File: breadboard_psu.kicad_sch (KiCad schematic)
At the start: 21 parts, among them J1 Barrel_Jack_MountingPin, J2 Conn_01x02, J3 Conn_01x02, J4 Conn_02x04_Odd_Even, J5 Conn_01x02, SW1 SW_DPDT_x2, SW2 SW_DPDT_x2, U1 LM317_TO-220

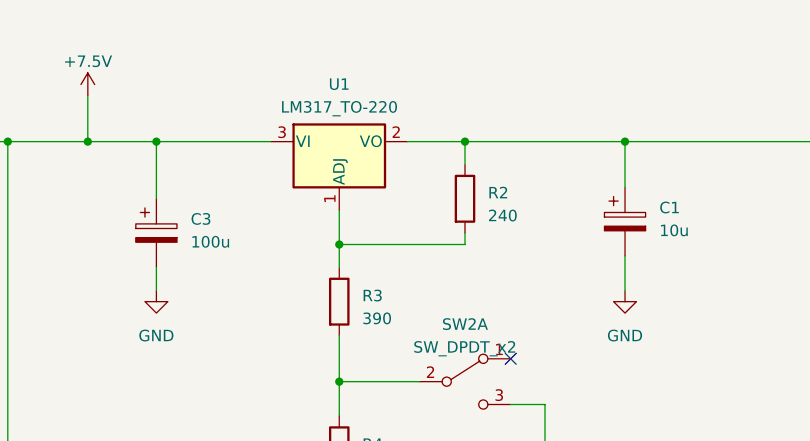
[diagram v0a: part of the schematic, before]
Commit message: MaJ TO220 a plat + esthétique
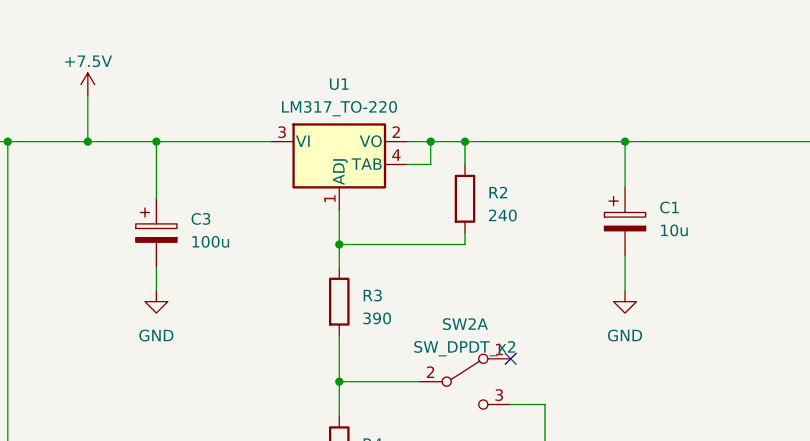
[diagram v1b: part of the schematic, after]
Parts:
- J1: footprint Connector_BarrelJack:BarrelJack_Kycon_KLDX-0202-xC_Horizontal -> Connector_BarrelJack:BarrelJack_Horizontal_PJ-002A
- U1: footprint Package_TO_SOT_THT:TO-220-3_Vertical -> Package_TO_SOT_THT:TO-220-3_Horizontal_TabDown_Connected; symbol Regulator_Linear:LM317_TO-220 -> MyLibrary:LM317_TO-220_TAB
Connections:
- net VCC: now also U1.4 (TAB)
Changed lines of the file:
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@@
     (company "Julien Boriasse")
+  )
+  (junction (at 170.18 88.9) (diameter 0) (color 0 0 0 0)
   )
   (junction (at 72.39 181.61) (diameter 0) (color 0 0 0 0)
@@
     (stroke (width 0) (type default))
   )
-  (wire (pts (xy 167.64 88.9) (xy 173.99 88.9))
+  (wire (pts (xy 167.64 88.9) (xy 170.18 88.9))
     (stroke (width 0) (type default))
   )
@@
     (stroke (width 0) (type default))
   )
+  (wire (pts (xy 170.18 91.44) (xy 170.18 88.9))
+    (stroke (width 0) (type default))
+  )
   (wire (pts (xy 281.94 88.9) (xy 255.27 88.9))
     (stroke (width 0) (type default))
@@
     (stroke (width 0) (type default))
   )
+  (wire (pts (xy 167.64 91.44) (xy 170.18 91.44))
+    (stroke (width 0) (type default))
+  )
   (wire (pts (xy 160.02 129.54) (xy 160.02 127))
     (stroke (width 0) (type default))
@@
   )
   (wire (pts (xy 123.19 125.73) (xy 123.19 88.9))
+    (stroke (width 0) (type default))
+  )
+  (wire (pts (xy 170.18 88.9) (xy 173.99 88.9))
     (stroke (width 0) (type default))
   )
@@
       (effects (font (size 1.27 1.27)))
     )
-    (property "Footprint" "Connector_BarrelJack:BarrelJack_Kycon_KLDX-0202-xC_Horizontal" (at 49.53 89.916 0)
+    (property "Footprint" "Connector_BarrelJack:BarrelJack_Horizontal_PJ-002A" (at 49.53 89.916 0)
       (effects (font (size 1.27 1.27)) hide)
     )
@@
     )
   )
-  (symbol (lib_id "Regulator_Linear:LM317_TO-220") (at 160.02 88.9 0) (unit 1)
+  (symbol (lib_id "MyLibrary:LM317_TO-220_TAB") (at 160.02 88.9 0) (unit 1)
     (in_bom yes) (on_board yes) (dnp no) (fields_autoplaced)
     (property "Reference" "U1" (at 160.02 82.55 0)
@@
       (effects (font (size 1.27 1.27)))
     )
-    (property "Footprint" "Package_TO_SOT_THT:TO-220-3_Vertical" (at 160.02 82.55 0)
+    (property "Footprint" "Package_TO_SOT_THT:TO-220-3_Horizontal_TabDown_Connected" (at 160.02 82.55 0)
       (effects (font (size 1.27 1.27) italic) hide)
     )
@@
     (pin "2")
     (pin "3")
-    (instances
-      (project "breadboard_psu"
+    (pin "4")
+    (instances
+      (project "breadboard_psu"

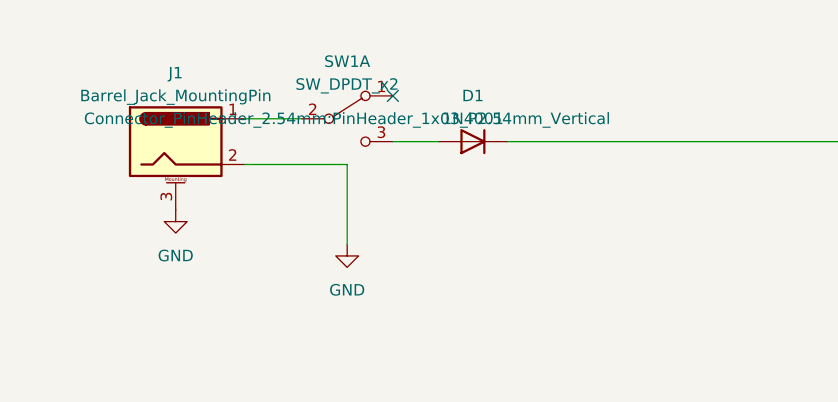
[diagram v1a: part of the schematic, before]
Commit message: Ajout MPN + BOM
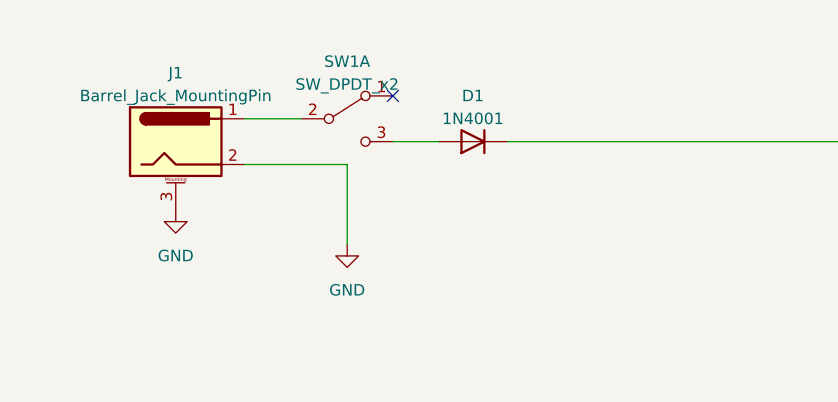
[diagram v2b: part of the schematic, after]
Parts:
- C1: SPN (none) -> 1189-3733-1-ND
- C2: SPN (none) -> BC1084CT-ND
- C3: SPN (none) -> 399-6650-1-ND
- D1: MPN (none) -> 1N4001-T; SPN (none) -> 1N4001DICT-ND
- J1: MPN (none) -> PJ-002A; SPN (none) -> CP-002A-ND
- U1: MPN (none) -> LM317KCS; SPN (none) -> 296-13869-5-ND
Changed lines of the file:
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@@
     )
     (property "Footprint" "Connector_PinHeader_2.54mm:PinHeader_1x03_P2.54mm_Vertical" (at 67.31 86.36 0)
-      (effects (font (size 1.27 1.27)))
+      (effects (font (size 1.27 1.27)) hide)
     )
     (property "Datasheet" "~" (at 67.31 86.36 0)
@@
       (effects (font (size 1.27 1.27)) hide)
     )
+    (property "MPN" "1N4001-T" (at 81.28 88.9 0)
+      (effects (font (size 1.27 1.27)) hide)
+    )
+    (property "SPN" "1N4001DICT-ND" (at 81.28 88.9 0)
+      (effects (font (size 1.27 1.27)) hide)
+    )
     (pin "1")
     (pin "2")
@@
       (effects (font (size 1.27 1.27)) hide)
     )
+    (property "SPN" "1189-3733-1-ND" (at 191.77 97.79 0)
+      (effects (font (size 1.27 1.27)) hide)
+    )
     (pin "1")
     (pin "2")
@@
       (effects (font (size 1.27 1.27)) hide)
     )
-    (property "Datasheet" "~" (at 49.53 89.916 0)
+    (property "Datasheet" "https://www.cuidevices.com/product/resource/pj-002a.pdf" (at 49.53 89.916 0)
+      (effects (font (size 1.27 1.27)) hide)
+    )
+    (property "SPN" "CP-002A-ND" (at 48.26 88.9 0)
+      (effects (font (size 1.27 1.27)) hide)
+    )
+    (property "MPN" "PJ-002A" (at 48.26 88.9 0)
       (effects (font (size 1.27 1.27)) hide)
     )
@@
       (effects (font (size 1.27 1.27)) hide)
     )
+    (property "SPN" "BC1084CT-ND" (at 215.9 97.79 0)
+      (effects (font (size 1.27 1.27)) hide)
+    )
     (pin "1")
     (pin "2")
@@
     )
     (property "Height" "12.50mm" (at 139.7 99.06 0)
+      (effects (font (size 1.27 1.27)) hide)
+    )
+    (property "SPN" "399-6650-1-ND" (at 139.7 99.06 0)
       (effects (font (size 1.27 1.27)) hide)
     )
@@
       (effects (font (size 1.27 1.27)) hide)
     )
+    (property "MPN" "LM317KCS" (at 160.02 88.9 0)
+      (effects (font (size 1.27 1.27)) hide)
+    )
+    (property "SPN" "296-13869-5-ND" (at 160.02 88.9 0)
+      (effects (font (size 1.27 1.27)) hide)
+    )

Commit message: DEL 5mm
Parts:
- D2: footprint LED_THT:LED_D3.0mm -> LED_THT:LED_D5.0mm
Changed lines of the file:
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@@
       (effects (font (size 1.27 1.27)) (justify right))
     )
-    (property "Footprint" "LED_THT:LED_D3.0mm" (at 232.41 104.14 0)
+    (property "Footprint" "LED_THT:LED_D5.0mm" (at 232.41 104.14 0)
       (effects (font (size 1.27 1.27)) hide)
     )

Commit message: 4 pin par tab
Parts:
- removed J2, J3: Conn_01x02, Connector_PinHeader_2.54mm:PinHeader_1x02_P2.54mm_Vertical, symbol Connector_Generic:Conn_01x02
- added J2, J3: Conn_02x02_Odd_Even, Connector_PinHeader_2.54mm:PinHeader_2x02_P2.54mm_Vertical, symbol Connector_Generic:Conn_02x02_Odd_Even
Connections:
- net GND: now also J2.3 (Pin_3), J2.4 (Pin_4), J3.3 (Pin_3), J3.4 (Pin_4)
- net VCC: now also J2.1 (Pin_1), J2.2 (Pin_2), J3.1 (Pin_1), J3.2 (Pin_2)

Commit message: Info des composants a jour
MPN SPN footprint 3D
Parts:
- C1: footprint Capacitor_THT:CP_Radial_D5.0mm_P2.50mm -> Library:CP_Radial_D5.0mm_P5.0mm_EEU-EB1J100SB; Height 8mm -> 12mm; MPN 35ML10MEFCT54X7 -> EEU-EB1J100SB; SPN 1189-3733-1-ND -> P19615CT-ND
- C2: footprint Capacitor_THT:C_Axial_L3.8mm_D2.6mm_P7.50mm_Horizontal -> Library:C_Rect_L4.0mm_W2.5mm_P5.00mm_RDER71H104K0K1H03B; MPN K104K15X7RF5TL2 -> RDER71H104K0K1H03B; SPN BC1084CT-ND -> 490-8814-ND
- C3: Height 12.50mm -> 5mm; MPN ESK107M025AE3EA -> ES5107M016AE1EA; SPN 399-6650-1-ND -> 399-6648-1-ND
- D1: MPN 1N4001-T -> 1N4001RLG; SPN 1N4001DICT-ND -> 1N4001RLGOSTR-ND
- D2: MPN (none) -> XLUG12D; SPN (none) -> 1497-1023-ND
- R2: SPN (none) -> 13-MFR-25FBF52-240R-ND
- R3: SPN (none) -> MFR-25FBF52-390R-ND
- R4: SPN (none) -> MFR-25FBF52-330R-ND
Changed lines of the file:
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@@
       (effects (font (size 1.27 1.27)) hide)
     )
-    (property "Datasheet" "~" (at 232.41 104.14 0)
+    (property "Datasheet" "https://www.sunledusa.com/products/spec/XLUG12D.pdf" (at 232.41 104.14 0)
+      (effects (font (size 1.27 1.27)) hide)
+    )
+    (property "SPN" "1497-1023-ND" (at 232.41 104.14 90)
+      (effects (font (size 1.27 1.27)) hide)
+    )
+    (property "MPN" "XLUG12D" (at 232.41 104.14 90)
       (effects (font (size 1.27 1.27)) hide)
     )
@@
       (effects (font (size 1.27 1.27)) hide)
     )
-    (property "Datasheet" "http://www.vishay.com/docs/88503/1n4001.pdf" (at 81.28 88.9 0)
+    (property "Datasheet" "https://www.onsemi.com/pdf/datasheet/1n4001-d.pdf" (at 81.28 88.9 0)
       (effects (font (size 1.27 1.27)) hide)
     )
@@
       (effects (font (size 1.27 1.27)) hide)
     )
-    (property "MPN" "1N4001-T" (at 81.28 88.9 0)
-      (effects (font (size 1.27 1.27)) hide)
-    )
-    (property "SPN" "1N4001DICT-ND" (at 81.28 88.9 0)
+    (property "MPN" "1N4001RLG" (at 81.28 88.9 0)
+      (effects (font (size 1.27 1.27)) hide)
+    )
+    (property "SPN" "1N4001RLGOSTR-ND" (at 81.28 88.9 0)
       (effects (font (size 1.27 1.27)) hide)
     )
@@
     )
     (property "Datasheet" "~" (at 160.02 106.68 0)
+      (effects (font (size 1.27 1.27)) hide)
+    )
+    (property "SPN" "MFR-25FBF52-390R-ND" (at 160.02 106.68 0)
       (effects (font (size 1.27 1.27)) hide)
     )
@@
       (effects (font (size 1.27 1.27)) (justify left))
     )
-    (property "Footprint" "Capacitor_THT:CP_Radial_D5.0mm_P2.50mm" (at 192.7352 101.6 0)
-      (effects (font (size 1.27 1.27)) hide)
-    )
-    (property "Datasheet" "~" (at 191.77 97.79 0)
-      (effects (font (size 1.27 1.27)) hide)
-    )
-    (property "MPN" "35ML10MEFCT54X7" (at 191.77 97.79 0)
-      (effects (font (size 1.27 1.27)) hide)
-    )
-    (property "Height" "8mm" (at 191.77 97.79 0)
-      (effects (font (size 1.27 1.27)) hide)
-    )
-    (property "SPN" "1189-3733-1-ND" (at 191.77 97.79 0)
+    (property "Footprint" "Library:CP_Radial_D5.0mm_P5.0mm_EEU-EB1J100SB" (at 192.7352 101.6 0)
+      (effects (font (size 1.27 1.27)) hide)
+    )
+    (property "Datasheet" "https://industrial.panasonic.com/cdbs/www-data/pdf/RDF0000/ABA0000C1024.pdf" (at 191.77 97.79 0)
+      (effects (font (size 1.27 1.27)) hide)
+    )
+    (property "MPN" "EEU-EB1J100SB" (at 191.77 97.79 0)
+      (effects (font (size 1.27 1.27)) hide)
+    )
+    (property "Height" "12mm" (at 191.77 97.79 0)
+      (effects (font (size 1.27 1.27)) hide)
+    )
+    (property "SPN" "P19615CT-ND" (at 191.77 97.79 0)
       (effects (font (size 1.27 1.27)) hide)
     )
@@
       (effects (font (size 1.27 1.27)) hide)
     )
+    (property "SPN" "13-MFR-25FBF52-240R-ND" (at 173.99 95.25 0)
+      (effects (font (size 1.27 1.27)) hide)
+    )
     (pin "1")
     (pin "2")
@@
       (effects (font (size 1.27 1.27)) (justify left))
     )
-    (property "Footprint" "Capacitor_THT:C_Axial_L3.8mm_D2.6mm_P7.50mm_Horizontal" (at 216.8652 101.6 0)
-      (effects (font (size 1.27 1.27)) hide)
-    )
-    (property "Datasheet" "~" (at 215.9 97.79 0)
-      (effects (font (size 1.27 1.27)) hide)
-    )
-    (property "MPN" "K104K15X7RF5TL2" (at 215.9 97.79 0)
-      (effects (font (size 1.27 1.27)) hide)
-    )
-    (property "SPN" "BC1084CT-ND" (at 215.9 97.79 0)
+    (property "Footprint" "Library:C_Rect_L4.0mm_W2.5mm_P5.00mm_RDER71H104K0K1H03B" (at 216.8652 101.6 0)
+      (effects (font (size 1.27 1.27)) hide)
+    )
+    (property "Datasheet" "https://search.murata.co.jp/Ceramy/image/img/A01X/G101/ENG/RDE_X7R_250V-1kV_E.pdf" (at 215.9 97.79 0)
+      (effects (font (size 1.27 1.27)) hide)
+    )
+    (property "MPN" "RDER71H104K0K1H03B" (at 215.9 97.79 0)
+      (effects (font (size 1.27 1.27)) hide)
+    )
+    (property "SPN" "490-8814-ND" (at 215.9 97.79 0)
       (effects (font (size 1.27 1.27)) hide)
     )
@@
       (effects (font (size 1.27 1.27)) hide)
     )
-    (property "MPN" "ESK107M025AE3EA" (at 139.7 99.06 0)
-      (effects (font (size 1.27 1.27)) hide)
-    )
-    (property "Height" "12.50mm" (at 139.7 99.06 0)
-      (effects (font (size 1.27 1.27)) hide)
-    )
-    (property "SPN" "399-6650-1-ND" (at 139.7 99.06 0)
+    (property "MPN" "ES5107M016AE1EA" (at 139.7 99.06 0)
+      (effects (font (size 1.27 1.27)) hide)
+    )
+    (property "Height" "5mm" (at 139.7 99.06 0)
+      (effects (font (size 1.27 1.27)) hide)
+    )
+    (property "SPN" "399-6648-1-ND" (at 139.7 99.06 0)
       (effects (font (size 1.27 1.27)) hide)
     )
@@
       (effects (font (size 1.27 1.27)) hide)
     )
+    (property "SPN" "MFR-25FBF52-330R-ND" (at 160.02 123.19 0)
+      (effects (font (size 1.27 1.27)) hide)
+    )

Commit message: Changement du silkscreen + Resistance & diode 300mils
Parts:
- D1: footprint Diode_THT:D_DO-41_SOD81_P10.16mm_Horizontal -> Diode_THT:D_DO-41_SOD81_P7.62mm_Horizontal
- R1, R2, R3, R4: footprint Resistor_THT:R_Axial_DIN0207_L6.3mm_D2.5mm_P10.16mm_Horizontal -> Resistor_THT:R_Axial_DIN0207_L6.3mm_D2.5mm_P7.62mm_Horizontal
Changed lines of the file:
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@@
       (effects (font (size 1.27 1.27)))
     )
-    (property "Footprint" "Diode_THT:D_DO-41_SOD81_P10.16mm_Horizontal" (at 81.28 88.9 0)
+    (property "Footprint" "Diode_THT:D_DO-41_SOD81_P7.62mm_Horizontal" (at 81.28 88.9 0)
       (effects (font (size 1.27 1.27)) hide)
     )
@@
       (effects (font (size 1.27 1.27)) (justify left))
     )
-    (property "Footprint" "Resistor_THT:R_Axial_DIN0207_L6.3mm_D2.5mm_P10.16mm_Horizontal" (at 158.242 106.68 90)
+    (property "Footprint" "Resistor_THT:R_Axial_DIN0207_L6.3mm_D2.5mm_P7.62mm_Horizontal" (at 158.242 106.68 90)
       (effects (font (size 1.27 1.27)) hide)
     )
@@
       (effects (font (size 1.27 1.27)) (justify left))
     )
-    (property "Footprint" "Resistor_THT:R_Axial_DIN0207_L6.3mm_D2.5mm_P10.16mm_Horizontal" (at 230.632 95.25 90)
+    (property "Footprint" "Resistor_THT:R_Axial_DIN0207_L6.3mm_D2.5mm_P7.62mm_Horizontal" (at 230.632 95.25 90)
       (effects (font (size 1.27 1.27)) hide)
     )
@@
       (effects (font (size 1.27 1.27)) (justify left))
     )
-    (property "Footprint" "Resistor_THT:R_Axial_DIN0207_L6.3mm_D2.5mm_P10.16mm_Horizontal" (at 172.212 95.25 90)
+    (property "Footprint" "Resistor_THT:R_Axial_DIN0207_L6.3mm_D2.5mm_P7.62mm_Horizontal" (at 172.212 95.25 90)
       (effects (font (size 1.27 1.27)) hide)
     )
@@
       (effects (font (size 1.27 1.27)) (justify left))
     )
-    (property "Footprint" "Resistor_THT:R_Axial_DIN0207_L6.3mm_D2.5mm_P10.16mm_Horizontal" (at 158.242 123.19 90)
-      (effects (font (size 1.27 1.27)) hide)
-    )
+    (property "Footprint" "Resistor_THT:R_Axial_DIN0207_L6.3mm_D2.5mm_P7.62mm_Horizontal" (at 158.242 123.19 90)
+      (effects (font (size 1.27 1.27)) hide)
+    )

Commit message: Cleanup
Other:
- note added: "VCC = 5V ou 3.3V selon la position du jumper sur SW2"
- note removed: "VCC = 5V or 3.3V depending on ADJ"
- title: Breadboard PSU -> Carte d'alimentation de prototypage
- moved on the sheet: C1, C2, C3, D1, D2, H1, H2, H3, H4, J1, J2, J3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

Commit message: Footprint oversized
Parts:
- C3: footprint Capacitor_THT:CP_Radial_D6.3mm_P2.50mm -> Library:CP_Radial_D6.3mm_P2.50mm_Oversized
- D1: footprint Diode_THT:D_DO-41_SOD81_P7.62mm_Horizontal -> Library:D_DO-41_SOD81_P7.62mm_Horizontal_Oversized
- D2: footprint LED_THT:LED_D5.0mm -> Library:LED_D5.0mm_Oversized
- J1: footprint Connector_BarrelJack:BarrelJack_Horizontal_PJ-002A -> Library:BarrelJack_Horizontal_PJ-002A_Oversized
- J2, J3: footprint Connector_PinHeader_2.54mm:PinHeader_2x02_P2.54mm_Vertical -> Library:PinHeader_2x02_P2.54mm_Vertical_Oversized
- J4: footprint Connector_PinHeader_2.54mm:PinHeader_2x04_P2.54mm_Vertical -> Library:PinHeader_2x04_P2.54mm_Vertical_Oversized
- J5: footprint Connector_PinSocket_2.54mm:PinSocket_1x02_P2.54mm_Vertical -> Library:PinSocket_1x02_P2.54mm_Vertical_Oversized
- R1, R2, R3, R4: footprint Resistor_THT:R_Axial_DIN0207_L6.3mm_D2.5mm_P7.62mm_Horizontal -> Library:R_Axial_DIN0207_L6.3mm_D2.5mm_P7.62mm_Horizontal_Oversized
- SW1, SW2: footprint Connector_PinHeader_2.54mm:PinHeader_1x03_P2.54mm_Vertical -> Library:PinHeader_1x03_P2.54mm_Vertical_Oversized
- U1: footprint Package_TO_SOT_THT:TO-220-3_Horizontal_TabDown_Connected -> Library:TO-220-3_Horizontal_TabDown_Connected_Oversized
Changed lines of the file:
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@@
       (effects (font (size 1.27 1.27)))
     )
-    (property "Footprint" "Connector_PinHeader_2.54mm:PinHeader_1x03_P2.54mm_Vertical" (at 189.23 105.41 0)
+    (property "Footprint" "Library:PinHeader_1x03_P2.54mm_Vertical_Oversized" (at 189.23 105.41 0)
       (effects (font (size 1.27 1.27)) hide)
     )
@@
       (effects (font (size 1.27 1.27)) (justify right))
     )
-    (property "Footprint" "LED_THT:LED_D5.0mm" (at 247.65 93.98 0)
+    (property "Footprint" "Library:LED_D5.0mm_Oversized" (at 247.65 93.98 0)
       (effects (font (size 1.27 1.27)) hide)
     )
@@
       (effects (font (size 1.27 1.27)))
     )
-    (property "Footprint" "Connector_PinHeader_2.54mm:PinHeader_1x03_P2.54mm_Vertical" (at 82.55 76.2 0)
+    (property "Footprint" "Library:PinHeader_1x03_P2.54mm_Vertical_Oversized" (at 82.55 76.2 0)
       (effects (font (size 1.27 1.27)) hide)
     )
@@
       (effects (font (size 1.27 1.27)))
     )
-    (property "Footprint" "Diode_THT:D_DO-41_SOD81_P7.62mm_Horizontal" (at 96.52 78.74 0)
+    (property "Footprint" "Library:D_DO-41_SOD81_P7.62mm_Horizontal_Oversized" (at 96.52 78.74 0)
       (effects (font (size 1.27 1.27)) hide)
     )
@@
       (effects (font (size 1.27 1.27)) (justify left))
     )
-    (property "Footprint" "Resistor_THT:R_Axial_DIN0207_L6.3mm_D2.5mm_P7.62mm_Horizontal" (at 173.482 96.52 90)
+    (property "Footprint" "Library:R_Axial_DIN0207_L6.3mm_D2.5mm_P7.62mm_Horizontal_Oversized" (at 173.482 96.52 90)
       (effects (font (size 1.27 1.27)) hide)
     )
@@
       (effects (font (size 1.27 1.27)) (justify left))
     )
-    (property "Footprint" "Resistor_THT:R_Axial_DIN0207_L6.3mm_D2.5mm_P7.62mm_Horizontal" (at 245.872 85.09 90)
+    (property "Footprint" "Library:R_Axial_DIN0207_L6.3mm_D2.5mm_P7.62mm_Horizontal_Oversized" (at 245.872 85.09 90)
       (effects (font (size 1.27 1.27)) hide)
     )
@@
       (effects (font (size 1.27 1.27)))
     )
-    (property "Footprint" "Connector_BarrelJack:BarrelJack_Horizontal_PJ-002A" (at 64.77 79.756 0)
+    (property "Footprint" "Library:BarrelJack_Horizontal_PJ-002A_Oversized" (at 64.77 79.756 0)
       (effects (font (size 1.27 1.27)) hide)
     )
@@
       (effects (font (size 1.27 1.27)) (justify left))
     )
-    (property "Footprint" "Resistor_THT:R_Axial_DIN0207_L6.3mm_D2.5mm_P7.62mm_Horizontal" (at 187.452 85.09 90)
+    (property "Footprint" "Library:R_Axial_DIN0207_L6.3mm_D2.5mm_P7.62mm_Horizontal_Oversized" (at 187.452 85.09 90)
       (effects (font (size 1.27 1.27)) hide)
     )
@@
       (effects (font (size 1.27 1.27)) (justify left))
     )
-    (property "Footprint" "Capacitor_THT:CP_Radial_D6.3mm_P2.50mm" (at 155.9052 92.71 0)
+    (property "Footprint" "Library:CP_Radial_D6.3mm_P2.50mm_Oversized" (at 155.9052 92.71 0)
       (effects (font (size 1.27 1.27)) hide)
     )
@@
       (effects (font (size 1.27 1.27)) (justify left))
     )
-    (property "Footprint" "Connector_PinSocket_2.54mm:PinSocket_1x02_P2.54mm_Vertical" (at 148.59 115.57 0)
+    (property "Footprint" "Library:PinSocket_1x02_P2.54mm_Vertical_Oversized" (at 148.59 115.57 0)
       (effects (font (size 1.27 1.27)) hide)
     )
@@
       (effects (font (size 1.27 1.27)))
     )
-    (property "Footprint" "Connector_PinHeader_2.54mm:PinHeader_2x02_P2.54mm_Vertical" (at 304.8 86.36 0)
+    (property "Footprint" "Library:PinHeader_2x02_P2.54mm_Vertical_Oversized" (at 304.8 86.36 0)
       (effects (font (size 1.27 1.27)) hide)
     )
@@
       (effects (font (size 1.27 1.27)))
     )
-    (property "Footprint" "Connector_PinHeader_2.54mm:PinHeader_2x02_P2.54mm_Vertical" (at 279.4 86.36 0)
+    (property "Footprint" "Library:PinHeader_2x02_P2.54mm_Vertical_Oversized" (at 279.4 86.36 0)
       (effects (font (size 1.27 1.27)) hide)
     )
@@
       (effects (font (size 1.27 1.27)) (justify left))
     )
-    (property "Footprint" "Resistor_THT:R_Axial_DIN0207_L6.3mm_D2.5mm_P7.62mm_Horizontal" (at 173.482 113.03 90)
+    (property "Footprint" "Library:R_Axial_DIN0207_L6.3mm_D2.5mm_P7.62mm_Horizontal_Oversized" (at 173.482 113.03 90)
       (effects (font (size 1.27 1.27)) hide)
     )
@@
       (effects (font (size 1.27 1.27)))
     )
-    (property "Footprint" "Package_TO_SOT_THT:TO-220-3_Horizontal_TabDown_Connected" (at 175.26 72.39 0)
+    (property "Footprint" "Library:TO-220-3_Horizontal_TabDown_Connected_Oversized" (at 175.26 72.39 0)
       (effects (font (size 1.27 1.27) italic) hide)
     )
@@
       (effects (font (size 1.27 1.27)))
     )
-    (property "Footprint" "Connector_PinHeader_2.54mm:PinHeader_2x04_P2.54mm_Vertical" (at 332.74 92.71 0)
-      (effects (font (size 1.27 1.27)) hide)
-    )
+    (property "Footprint" "Library:PinHeader_2x04_P2.54mm_Vertical_Oversized" (at 332.74 92.71 0)
+      (effects (font (size 1.27 1.27)) hide)
+    )
